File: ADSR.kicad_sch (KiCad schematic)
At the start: 46 parts, among them K5 SW_SPDT, P15 1M, P17 R_POT, P18 1M, P6 10k, Q10 BC184, Q11 BC184, Q12 BC184, Q13 BC184, Q14 BC184, Q9 BC184, U11 UA747, U7 UA747

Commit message: Fix PCB errors
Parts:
- added C_Sin1 (x10): Conn_01x01, Connector_PinHeader_2.54mm:PinHeader_1x01_P2.54mm_Vertical, symbol Connector_Generic:Conn_01x01
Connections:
- net at P15.1, P15.2, Q9.2 (C)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: now also C_Sin1.1 (Pin_1)
- net at K5.2 (B), R49.1, U7.2 (+): now also C_Sin1.1 (Pin_1)
- net at P6.2, U7.6 (+): now also C_Sin1.1 (Pin_1)
- net at P6.1, RV56.1, RV56.2: now also C_Sin1.1 (Pin_1)
- net at P17.1, P17.2, Q9.3 (E): now also C_Sin1.1 (Pin_1)
- net at P15.3, R52.1: now also C_Sin1.1 (Pin_1)
- net at P17.3, R57.1: now also C_Sin1.1 (Pin_1)
- net at K5.3 (C), R47.2, R48.1: now also C_Sin1.1 (Pin_1)
- net at P18.1, P18.2, Q11.2 (C): now also C_Sin1.1 (Pin_1)
- net at P18.3, R54.1: now also C_Sin1.1 (Pin_1)
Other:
- moved on the sheet: D4, D5, D6, P18, P6, R52, R54, R57

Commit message: Kicad update
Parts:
- renumbered C_Sin1 to K5-2, C_Sin1 to K5-3, C_Sin1 to P15-1, C_Sin1 to P15-1-3, C_Sin1 to P16-1, C_Sin1 to P16-3, C_Sin1 to P17-1-3, C_Sin1 to P17-2, C_Sin1 to P18-1, C_Sin1 to P18-1-3

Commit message: Replace symbols with new library
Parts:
- C12: footprint Capacitor_THT:CP_Radial_D6.3mm_P2.50mm -> (none)
- C13: footprint Capacitor_THT:C_Disc_D5.0mm_W2.5mm_P5.00mm -> (none)
- D3, D4, D5, D6, D7: footprint Diode_THT:D_A-405_P10.16mm_Horizontal -> (none)
- K5, P15, P17, P18, P6: footprint Connector_PinSocket_2.54mm:PinSocket_1x03_P2.54mm_Vertical -> (none)
- K5-2, K5-3, P15-1, P15-1-3, P16-1, P16-3, P17-1-3, P17-2, P18-1, P18-1-3: footprint Connector_PinHeader_2.54mm:PinHeader_1x01_P2.54mm_Vertical -> (none)
- Q10, Q11, Q13, Q14, Q9: symbol Device:Q_NPN_BCE -> Transistor_BJT:Q_NPN_BCE
- Q12: symbol Device:Q_NPN_BCE -> Transistor_BJT:Q_NPN_CBE
- R47, R48, R49, R50, R51, R52, R53, R54, R55, R57, R58, R59, R60, R61, R62, R63, R64, R65, R66, R67, R68, R69, R70, R71, R72: footprint Resistor_THT:R_Axial_DIN0207_L6.3mm_D2.5mm_P15.24mm_Horizontal -> (none)
- RV56: footprint Potentiometer_THT:Potentiometer_Bourns_3296W_Vertical -> (none)
- U11, U7: footprint Package_DIP:DIP-14_W7.62mm_Socket_LongPads -> (none)
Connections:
- net at R62.1, R71.2: now also Q12.2 (B); no longer Q12.1 (B)
- net at R63.2, R64.1, R67.2: now also Q12.1 (C); no longer Q12.2 (C)

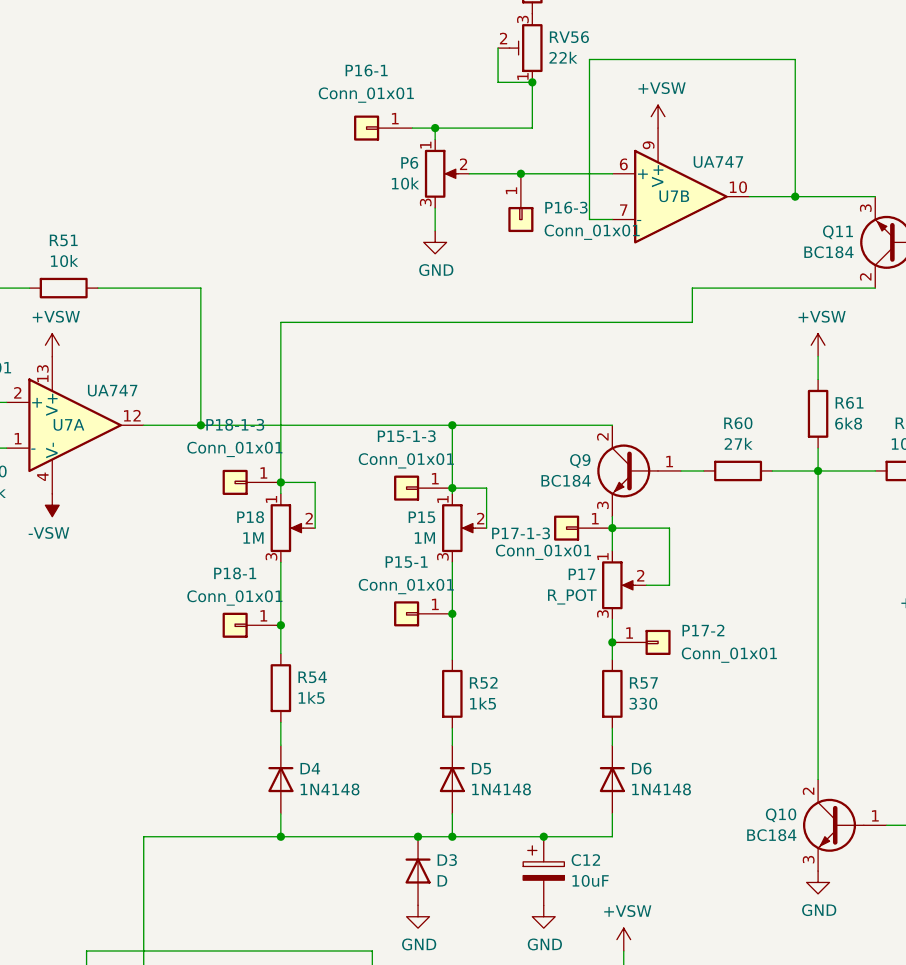
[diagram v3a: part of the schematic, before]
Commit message: Label connectors, update footprints
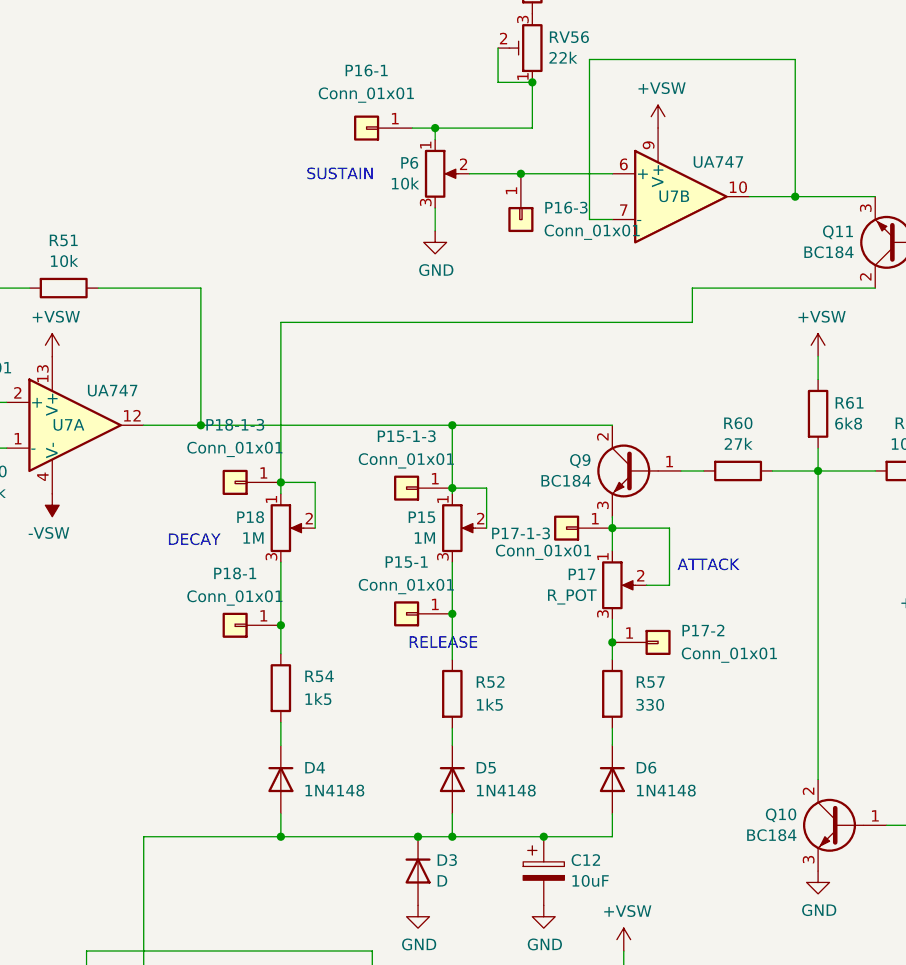
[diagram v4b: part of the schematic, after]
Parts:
- C12: footprint (none) -> Capacitor_THT:CP_Radial_D6.3mm_P2.50mm
- C13: footprint (none) -> Capacitor_THT:C_Disc_D5.0mm_W2.5mm_P5.00mm
- D3, D4, D5, D6, D7: footprint (none) -> Diode_THT:D_A-405_P10.16mm_Horizontal
- K5-2, K5-3, P15-1, P15-1-3, P16-1, P16-3, P17-1-3, P17-2, P18-1, P18-1-3: footprint (none) -> Connector_PinHeader_2.54mm:PinHeader_1x01_P2.54mm_Vertical
- R47, R48, R49, R50, R51, R52, R53, R54, R55, R57, R58, R59, R60, R61, R62, R63, R64, R65, R66, R67, R68, R69, R70, R71, R72: footprint (none) -> Resistor_THT:R_Axial_DIN0207_L6.3mm_D2.5mm_P15.24mm_Horizontal
- RV56: footprint (none) -> Potentiometer_THT:Potentiometer_Bourns_3296W_Vertical
- U11, U7: footprint (none) -> Package_DIP:DIP-14_W7.62mm_Socket_LongPads
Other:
- note added: "ATTACK"
- note added: "DECAY"
- note added: "RELEASE"
- note added: "SUSTAIN"
